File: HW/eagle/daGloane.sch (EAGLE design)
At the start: 61 parts, among them IC1 MCP1252-33X50, U1 STM32F10XTXU6, X2 USB-MICROB

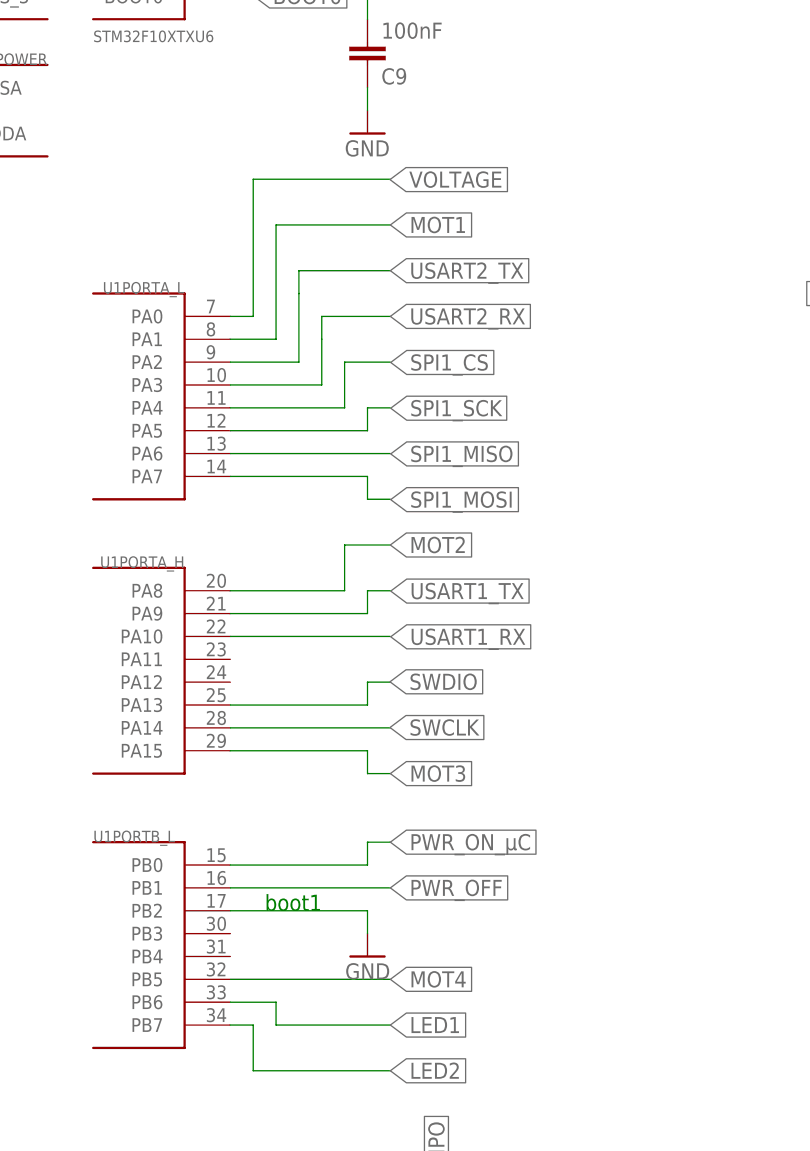
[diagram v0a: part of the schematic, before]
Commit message: pin assignment of µC changed  pwm outputs for the motors are now on PB0,PB1,PB4 and PB5. Those I/Os can be used with TIM3
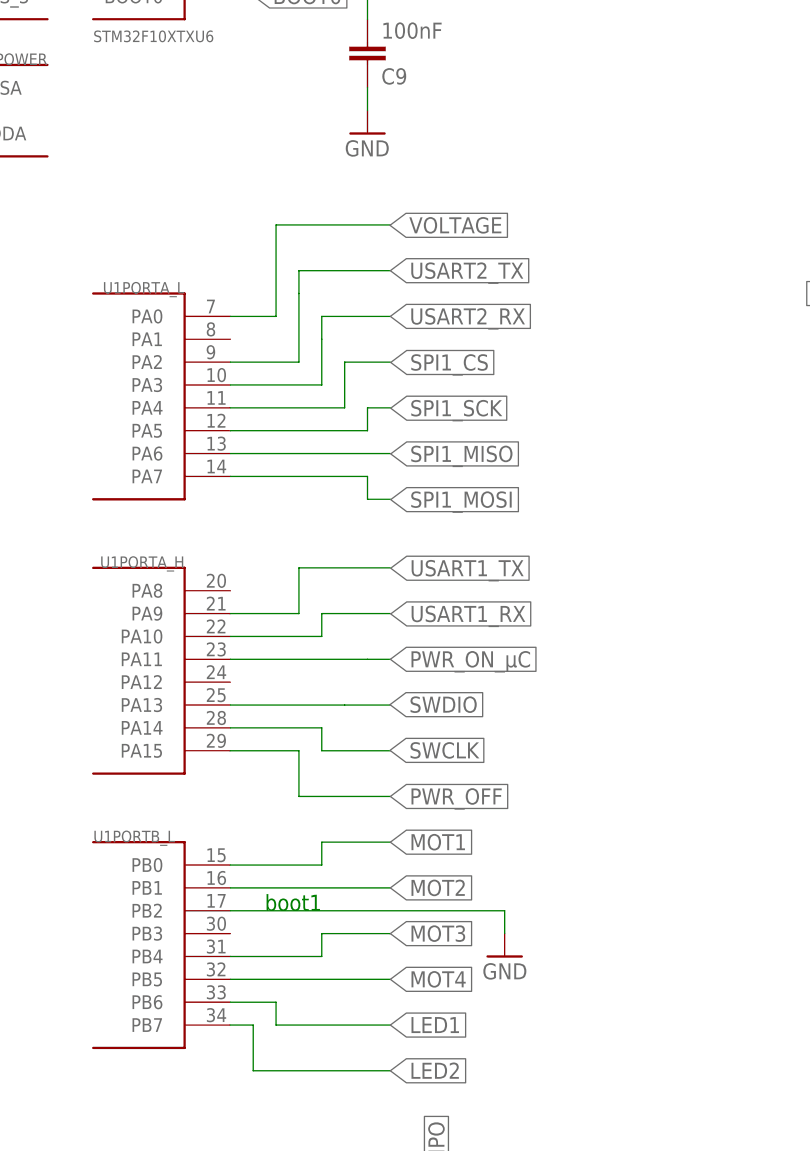
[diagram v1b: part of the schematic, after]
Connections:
- removed net MOT1: U1PORTA_L.PA1
- removed net MOT2: U1PORTA_H.PA8
- removed net MOT3: U1PORTA_H.PA15
- net PWR_OFF: no longer U1PORTB_L.PB1
- net PWR_ON_µC: no longer U1PORTB_L.PB0
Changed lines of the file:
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@@
 <instance part="GND51" gate="1" x="55.88" y="160.02"/>
 <instance part="3.3V6" gate="VCC" x="48.26" y="180.34" rot="MR0"/>
-<instance part="GND1" gate="1" x="116.84" y="83.82" rot="MR0"/>
+<instance part="GND1" gate="1" x="132.08" y="83.82" rot="MR0"/>
 <instance part="GND6" gate="1" x="116.84" y="17.78" rot="MR0"/>
 <instance part="X2" gate="G$1" x="233.68" y="66.04" rot="R180"/>
@@
 </segment>
 <segment>
-<wire x1="116.84" y1="86.36" x2="116.84" y2="88.9" width="0.1524" layer="91"/>
-<wire x1="116.84" y1="88.9" x2="101.6" y2="88.9" width="0.1524" layer="91"/>
+<wire x1="132.08" y1="86.36" x2="132.08" y2="88.9" width="0.1524" layer="91"/>
+<wire x1="132.08" y1="88.9" x2="101.6" y2="88.9" width="0.1524" layer="91"/>
 <pinref part="GND1" gate="1" pin="GND"/>
 <pinref part="U1" gate="PORTB_L" pin="PB2"/>
@@
 </segment>
 <segment>
-<wire x1="119.38" y1="170.18" x2="104.14" y2="170.18" width="0.1524" layer="91"/>
-<wire x1="104.14" y1="170.18" x2="104.14" y2="154.94" width="0.1524" layer="91"/>
-<wire x1="104.14" y1="154.94" x2="101.6" y2="154.94" width="0.1524" layer="91"/>
-<label x="119.34" y="170.14" size="1.778" layer="95" rot="MR180" xref="yes"/>
+<wire x1="119.38" y1="165.1" x2="106.68" y2="165.1" width="0.1524" layer="91"/>
+<wire x1="106.68" y1="165.1" x2="106.68" y2="154.94" width="0.1524" layer="91"/>
+<wire x1="106.68" y1="154.94" x2="101.6" y2="154.94" width="0.1524" layer="91"/>
+<label x="119.34" y="165.06" size="1.778" layer="95" rot="MR180" xref="yes"/>
 <pinref part="U1" gate="PORTA_L" pin="PA0"/>
 </segment>
@@
 </segment>
 <segment>
-<wire x1="119.38" y1="114.3" x2="116.84" y2="114.3" width="0.1524" layer="91"/>
-<wire x1="116.84" y1="114.3" x2="116.84" y2="111.76" width="0.1524" layer="91"/>
-<wire x1="116.84" y1="111.76" x2="101.6" y2="111.76" width="0.1524" layer="91"/>
-<label x="119.34" y="114.34" size="1.778" layer="95" xref="yes"/>
+<wire x1="119.38" y1="111.76" x2="114.3" y2="111.76" width="0.1524" layer="91"/>
+<wire x1="114.3" y1="111.76" x2="101.6" y2="111.76" width="0.1524" layer="91"/>
+<label x="119.34" y="111.8" size="1.778" layer="95" xref="yes"/>
 <pinref part="U1" gate="PORTA_H" pin="PA13"/>
 </segment>
@@
 </segment>
 <segment>
-<wire x1="119.38" y1="109.22" x2="101.6" y2="109.22" width="0.1524" layer="91"/>
-<label x="119.34" y="109.26" size="1.778" layer="95" xref="yes"/>
+<wire x1="119.38" y1="106.68" x2="111.76" y2="106.68" width="0.1524" layer="91"/>
+<wire x1="111.76" y1="106.68" x2="111.76" y2="109.22" width="0.1524" layer="91"/>
+<wire x1="111.76" y1="109.22" x2="101.6" y2="109.22" width="0.1524" layer="91"/>
+<label x="119.34" y="106.72" size="1.778" layer="95" xref="yes"/>
 <pinref part="U1" gate="PORTA_H" pin="PA14"/>
 </segment>
@@
 </segment>
 <segment>
-<wire x1="101.6" y1="121.92" x2="116.84" y2="121.92" width="0.1524" layer="91"/>
-<wire x1="116.84" y1="121.92" x2="116.84" y2="124.46" width="0.1524" layer="91"/>
-<wire x1="116.84" y1="124.46" x2="119.38" y2="124.46" width="0.1524" layer="91"/>
-<label x="119.42" y="124.42" size="1.778" layer="95" rot="MR180" xref="yes"/>
+<wire x1="101.6" y1="121.92" x2="109.22" y2="121.92" width="0.1524" layer="91"/>
+<wire x1="109.22" y1="121.92" x2="109.22" y2="127" width="0.1524" layer="91"/>
+<wire x1="109.22" y1="127" x2="119.38" y2="127" width="0.1524" layer="91"/>
+<label x="119.42" y="126.96" size="1.778" layer="95" rot="MR180" xref="yes"/>
 <pinref part="U1" gate="PORTA_H" pin="PA9"/>
 </segment>
@@
 </segment>
 <segment>
-<wire x1="101.6" y1="119.38" x2="119.38" y2="119.38" width="0.1524" layer="91"/>
-<label x="119.42" y="119.34" size="1.778" layer="95" rot="MR180" xref="yes"/>
+<wire x1="101.6" y1="119.38" x2="111.76" y2="119.38" width="0.1524" layer="91"/>
+<wire x1="111.76" y1="119.38" x2="111.76" y2="121.92" width="0.1524" layer="91"/>
+<wire x1="111.76" y1="121.92" x2="119.38" y2="121.92" width="0.1524" layer="91"/>
+<label x="119.42" y="121.88" size="1.778" layer="95" rot="MR180" xref="yes"/>
 <pinref part="U1" gate="PORTA_H" pin="PA10"/>
 </segment>
@@
 </segment>
 <segment>
-<wire x1="101.6" y1="91.44" x2="119.38" y2="91.44" width="0.1524" layer="91"/>
-<label x="119.38" y="91.44" size="1.778" layer="95" rot="MR180" xref="yes"/>
-<pinref part="U1" gate="PORTB_L" pin="PB1"/>
+<wire x1="101.6" y1="106.68" x2="109.22" y2="106.68" width="0.1524" layer="91"/>
+<wire x1="109.22" y1="106.68" x2="109.22" y2="101.6" width="0.1524" layer="91"/>
+<wire x1="109.22" y1="101.6" x2="119.38" y2="101.6" width="0.1524" layer="91"/>
+<label x="119.38" y="101.6" size="1.778" layer="95" rot="MR180" xref="yes"/>
 </segment>
 </net>
@@
 </segment>
 <segment>
-<wire x1="101.6" y1="93.98" x2="116.84" y2="93.98" width="0.1524" layer="91"/>
-<wire x1="116.84" y1="93.98" x2="116.84" y2="96.52" width="0.1524" layer="91"/>
-<wire x1="116.84" y1="96.52" x2="119.38" y2="96.52" width="0.1524" layer="91"/>
-<label x="119.38" y="96.52" size="1.778" layer="95" rot="MR180" xref="yes"/>
-<pinref part="U1" gate="PORTB_L" pin="PB0"/>
+<wire x1="101.6" y1="116.84" x2="116.84" y2="116.84" width="0.1524" layer="91"/>
+<wire x1="116.84" y1="116.84" x2="119.38" y2="116.84" width="0.1524" layer="91"/>
+<label x="119.38" y="116.84" size="1.778" layer="95" rot="MR180" xref="yes"/>
 </segment>
 </net>
@@
 <net name="MOT2" class="0">
 <segment>
-<pinref part="U1" gate="PORTA_H" pin="PA8"/>
-<wire x1="101.6" y1="124.46" x2="114.3" y2="124.46" width="0.1524" layer="91"/>
-<wire x1="114.3" y1="124.46" x2="114.3" y2="129.54" width="0.1524" layer="91"/>
-<wire x1="114.3" y1="129.54" x2="119.38" y2="129.54" width="0.1524" layer="91"/>
-<label x="119.38" y="129.54" size="1.778" layer="95" xref="yes"/>
+<wire x1="101.6" y1="91.44" x2="119.38" y2="91.44" width="0.1524" layer="91"/>
+<label x="119.38" y="91.44" size="1.778" layer="95" xref="yes"/>
 </segment>
 </net>
 <net name="MOT3" class="0">
 <segment>
-<pinref part="U1" gate="PORTA_H" pin="PA15"/>
-<wire x1="101.6" y1="106.68" x2="116.84" y2="106.68" width="0.1524" layer="91"/>
-<wire x1="116.84" y1="106.68" x2="116.84" y2="104.14" width="0.1524" layer="91"/>
-<wire x1="116.84" y1="104.14" x2="119.38" y2="104.14" width="0.1524" layer="91"/>
-<label x="119.38" y="104.14" size="1.778" layer="95" xref="yes"/>
+<wire x1="101.6" y1="83.82" x2="111.76" y2="83.82" width="0.1524" layer="91"/>
+<wire x1="111.76" y1="83.82" x2="111.76" y2="86.36" width="0.1524" layer="91"/>
+<wire x1="111.76" y1="86.36" x2="119.38" y2="86.36" width="0.1524" layer="91"/>
+<label x="119.38" y="86.36" size="1.778" layer="95" xref="yes"/>
 </segment>
 </net>
 <net name="MOT1" class="0">
 <segment>
-<pinref part="U1" gate="PORTA_L" pin="PA1"/>
-<wire x1="101.6" y1="152.4" x2="106.68" y2="152.4" width="0.1524" layer="91"/>
-<wire x1="106.68" y1="152.4" x2="106.68" y2="165.1" width="0.1524" layer="91"/>
-<wire x1="106.68" y1="165.1" x2="119.38" y2="165.1" width="0.1524" layer="91"/>
-<label x="119.38" y="165.1" size="1.778" layer="95" xref="yes"/>
-</segment>
-</net>
+<wire x1="101.6" y1="93.98" x2="111.76" y2="93.98" width="0.1524" layer="91"/>
+<wire x1="111.76" y1="93.98" x2="111.76" y2="96.52" width="0.1524" layer="91"/>
+<wire x1="111.76" y1="96.52" x2="119.38" y2="96.52" width="0.1524" layer="91"/>
+<label x="119.38" y="96.52" size="1.778" layer="95" xref="yes"/>
+</segment>
+</net>

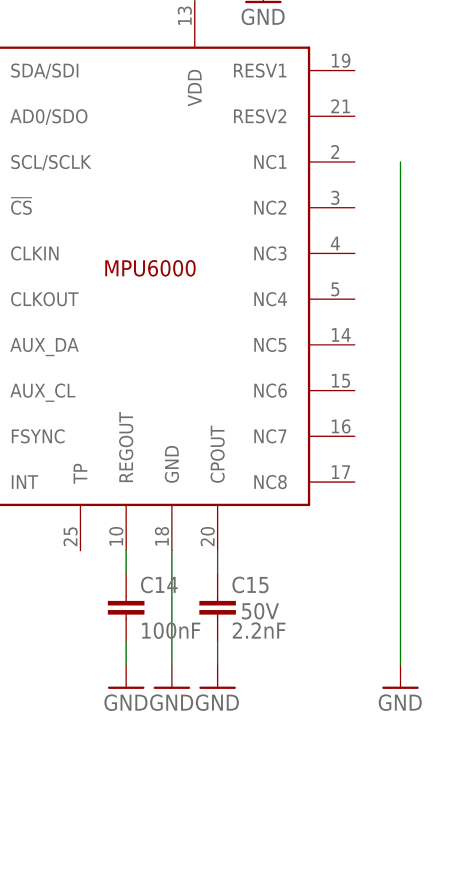
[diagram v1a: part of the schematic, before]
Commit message: gnd removed
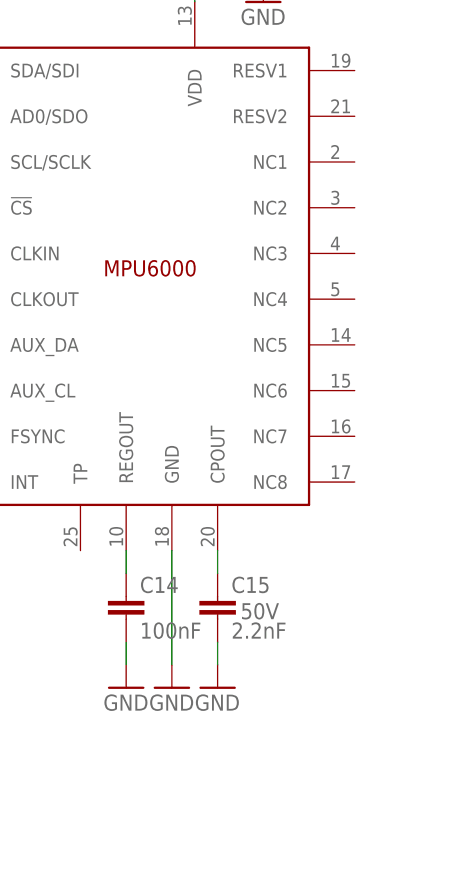
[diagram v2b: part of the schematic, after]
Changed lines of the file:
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@@
 <part name="R9" library="rcl" deviceset="R-EU_" device="R0603" value="1k"/>
 <part name="R10" library="rcl" deviceset="R-EU_" device="R0603" value="1k"/>
-<part name="GND24" library="supply1" deviceset="GND" device=""/>
 <part name="LED3" library="led" deviceset="LED" device="CHIPLED_0805"/>
 <part name="LED4" library="led" deviceset="LED" device="CHIPLED_0805"/>
@@
 <instance part="R9" gate="G$1" x="353.06" y="68.58"/>
 <instance part="R10" gate="G$1" x="353.06" y="60.96"/>
-<instance part="GND24" gate="1" x="375.92" y="154.94"/>
 <instance part="LED3" gate="G$1" x="172.72" y="33.02"/>
 <instance part="LED4" gate="G$1" x="185.42" y="33.02"/>
@@
 </segment>
 <segment>
-<wire x1="375.92" y1="213.36" x2="375.92" y2="208.28" width="0.1524" layer="91"/>
-<wire x1="375.92" y1="208.28" x2="375.92" y2="203.2" width="0.1524" layer="91"/>
-<wire x1="375.92" y1="203.2" x2="375.92" y2="198.12" width="0.1524" layer="91"/>
-<wire x1="375.92" y1="198.12" x2="375.92" y2="193.04" width="0.1524" layer="91"/>
-<wire x1="375.92" y1="193.04" x2="375.92" y2="187.96" width="0.1524" layer="91"/>
-<wire x1="375.92" y1="187.96" x2="375.92" y2="182.88" width="0.1524" layer="91"/>
-<wire x1="375.92" y1="182.88" x2="375.92" y2="177.8" width="0.1524" layer="91"/>
-<wire x1="375.92" y1="177.8" x2="375.92" y2="157.48" width="0.1524" layer="91"/>
-<pinref part="GND24" gate="1" pin="GND"/>
-</segment>
-<segment>

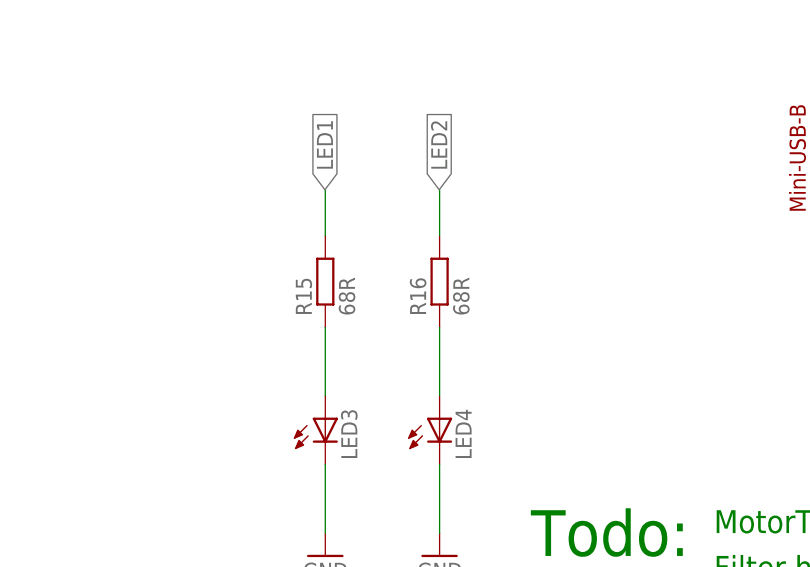
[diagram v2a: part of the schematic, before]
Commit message: all non standart part replaced by parts found in the daGloane.lbr library
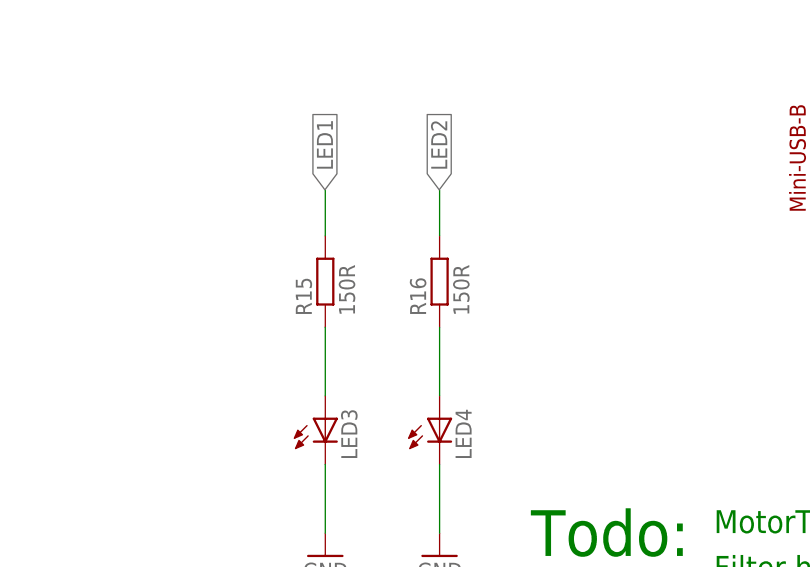
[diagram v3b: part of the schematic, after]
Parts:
- GND, SWCLK, SWDIO: device bldc_can:TESTPAD_TPB1,27 -> daGloane:TESTPAD_TPB1,27
- IC1: device microchip-MCP125x-xxx:MCP1252-33X50 -> daGloane:MCP1252-33X50
- ON/OFF: device SparkFun-Electromechanical:SWITCH-MOMENTARY-2SMD -> daGloane:SWITCH-MOMENTARY-2SMD
- R15, R16: value 68R -> 150R
- U$1: device canBLC2:MURATA-FILTER_CSTCE__G -> daGloane:MURATA-FILTER_CSTCE__G
- U$2: device LiPo-USB-Charger-v21:SPARKFUN_MCP73831 -> daGloane:SPARKFUN_MCP73831
- U$3: device MPU6000:MPU6000 -> daGloane:MPU6000
- U$4: device ftdiftx:SERIAL_FT230XQ -> daGloane:SERIAL_FT230XQ
- U1: device stm32:STM32F10XTXU6 -> daGloane:STM32F10XTXU6
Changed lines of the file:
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@@
 </classes>
 <parts>
-<part name="R16" library="rcl" deviceset="R-EU_" device="R0603" value="68R"/>
+<part name="R16" library="rcl" deviceset="R-EU_" device="R0603" value="150R"/>
 <part name="R20" library="rcl" deviceset="R-EU_" device="R0603" value="10k"/>
 <part name="GND12" library="supply1" deviceset="GND" device=""/>
@@
 <part name="R18" library="rcl" deviceset="R-EU_" device="R0603" value="3k3"/>
 <part name="C20" library="rcl" deviceset="C-EU" device="C0603" value="100nF"/>
-<part name="R15" library="rcl" deviceset="R-EU_" device="R0603" value="68R"/>
+<part name="R15" library="rcl" deviceset="R-EU_" device="R0603" value="150R"/>
 <part name="BOOTMD" library="SparkFun" deviceset="JUMPER-2" device="PTH"/>
 <part name="GND41" library="supply1" deviceset="GND" device=""/>
@@
 <part name="FRAME2" library="frames" deviceset="A3L-LOC" device=""/>
 <part name="3.3V" library="supply1" deviceset="VCC" device="" value="3.3V"/>
-<part name="SWDIO" library="bldc_can" deviceset="TESTPAD_TP" device="B1,27"/>
-<part name="SWCLK" library="bldc_can" deviceset="TESTPAD_TP" device="B1,27"/>
-<part name="GND" library="bldc_can" deviceset="TESTPAD_TP" device="B1,27"/>
+<part name="SWDIO" library="daGloane" deviceset="TESTPAD_TP" device="B1,27"/>
+<part name="SWCLK" library="daGloane" deviceset="TESTPAD_TP" device="B1,27"/>
+<part name="GND" library="daGloane" deviceset="TESTPAD_TP" device="B1,27"/>
 <part name="GND2" library="supply1" deviceset="GND" device=""/>
-<part name="U$3" library="MPU6000" deviceset="MPU6000" device=""/>
-<part name="U$4" library="ftdiftx" deviceset="SERIAL_FT230XQ" device=""/>
+<part name="U$3" library="daGloane" deviceset="MPU6000" device=""/>
+<part name="U$4" library="daGloane" deviceset="SERIAL_FT230XQ" device=""/>
 <part name="R14" library="rcl" deviceset="R-EU_" device="R0603" value="150R"/>
 <part name="R19" library="rcl" deviceset="R-EU_" device="R0603" value="150R"/>
@@
 <part name="LED1" library="led" deviceset="LED" device="CHIPLED_0805"/>
 <part name="LED2" library="led" deviceset="LED" device="CHIPLED_0805"/>
-<part name="U$2" library="LiPo-USB-Charger-v21" deviceset="SPARKFUN_MCP73831" device=""/>
+<part name="U$2" library="daGloane" deviceset="SPARKFUN_MCP73831" device=""/>
 <part name="C6" library="rcl" deviceset="C-EU" device="C0603" value="1µF"/>
 <part name="GND28" library="supply1" deviceset="GND" device=""/>
@@
 <part name="LIPO-" library="testpad" deviceset="TPS" device="PAD1-13Y"/>
 <part name="R2" library="rcl" deviceset="R-EU_" device="R0603" value="2k"/>
-<part name="IC1" library="microchip-MCP125x-xxx" deviceset="MCP1252-33X50" device=""/>
+<part name="IC1" library="daGloane" deviceset="MCP1252-33X50" device=""/>
 <part name="C13" library="rcl" deviceset="C-EU" device="C0805" value="10µF/6.3V"/>
 <part name="C12" library="rcl" deviceset="C-EU" device="C0805" value="10µF/6.3V"/>
@@
 <part name="C8" library="rcl" deviceset="C-EU" device="C0603" value="1µF"/>
 <part name="3.3V4" library="supply1" deviceset="VCC" device="" value="3.3V"/>
-<part name="ON/OFF" library="SparkFun-Electromechanical" deviceset="SWITCH-MOMENTARY-2" device="SMD"/>
+<part name="ON/OFF" library="daGloane" deviceset="SWITCH-MOMENTARY-2" device="SMD"/>
 <part name="D1" library="diode" deviceset="MBR0520LT" device=""/>
 <part name="R7" library="rcl" deviceset="R-EU_" device="R0603" value="10k"/>
@@
 <part name="R8" library="rcl" deviceset="R-EU_" device="R0603" value="10k"/>
 <part name="GND36" library="supply1" deviceset="GND" device=""/>
-<part name="U1" library="stm32" deviceset="STM32F10XTXU6" device=""/>
-<part name="U$1" library="canBLC2" deviceset="MURATA-FILTER_CSTCE__G" device=""/>
+<part name="U1" library="daGloane" deviceset="STM32F10XTXU6" device=""/>
+<part name="U$1" library="daGloane" deviceset="MURATA-FILTER_CSTCE__G" device=""/>
 <part name="GND37" library="supply1" deviceset="GND" device=""/>
 <part name="C9" library="rcl" deviceset="C-EU" device="C0603" value="100nF"/>

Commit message: micro USB b connector added to daGloane lbr
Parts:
- X2: value USB-MICROB -> SPARKFUN-CONNECTORS_USB-MICROB; device SparkFun-Connectors:USB-MICROB -> daGloane:SPARKFUN-CONNECTORS_USB-MICROB
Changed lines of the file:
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@@
 <part name="GND1" library="supply1" deviceset="GND" device=""/>
 <part name="GND6" library="supply1" deviceset="GND" device=""/>
-<part name="X2" library="SparkFun-Connectors" deviceset="USB" device="-MICROB"/>
+<part name="X2" library="daGloane" deviceset="SPARKFUN-CONNECTORS_USB" device="-MICROB"/>
 </parts>
 <sheets>
